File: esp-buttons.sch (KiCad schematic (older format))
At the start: 33 parts, among them Q1 FDV304P, U1 ESP-07v2, U2 LD1117S33CTR

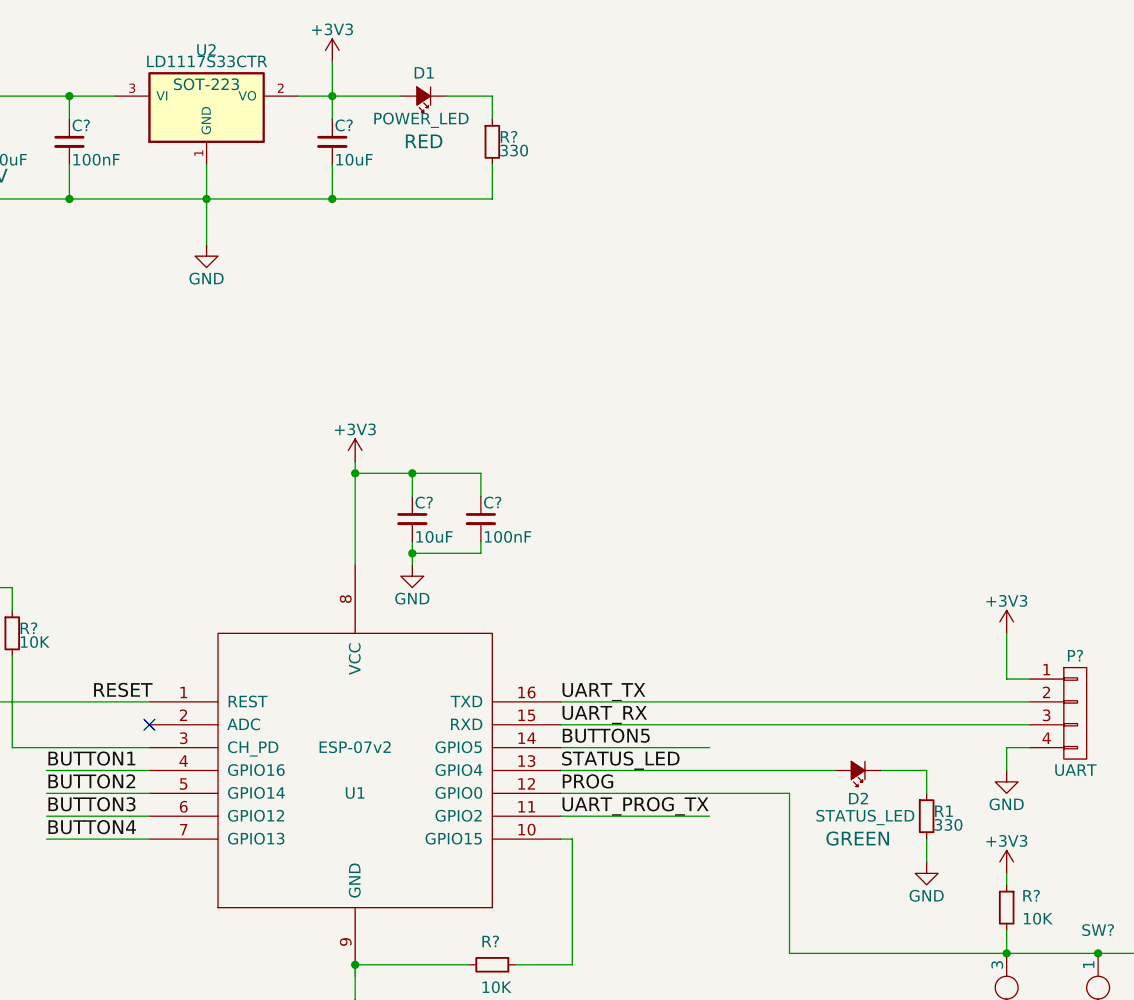
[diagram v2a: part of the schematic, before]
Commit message: Changed the value of the LEDs' resistors to give aproximately 5 mA of current to the LEDs. Changed the package of the SMD regulator (LD1117ADT33TR) from SOT-223 to TO-263 (D-PAK) for increased power dissipation
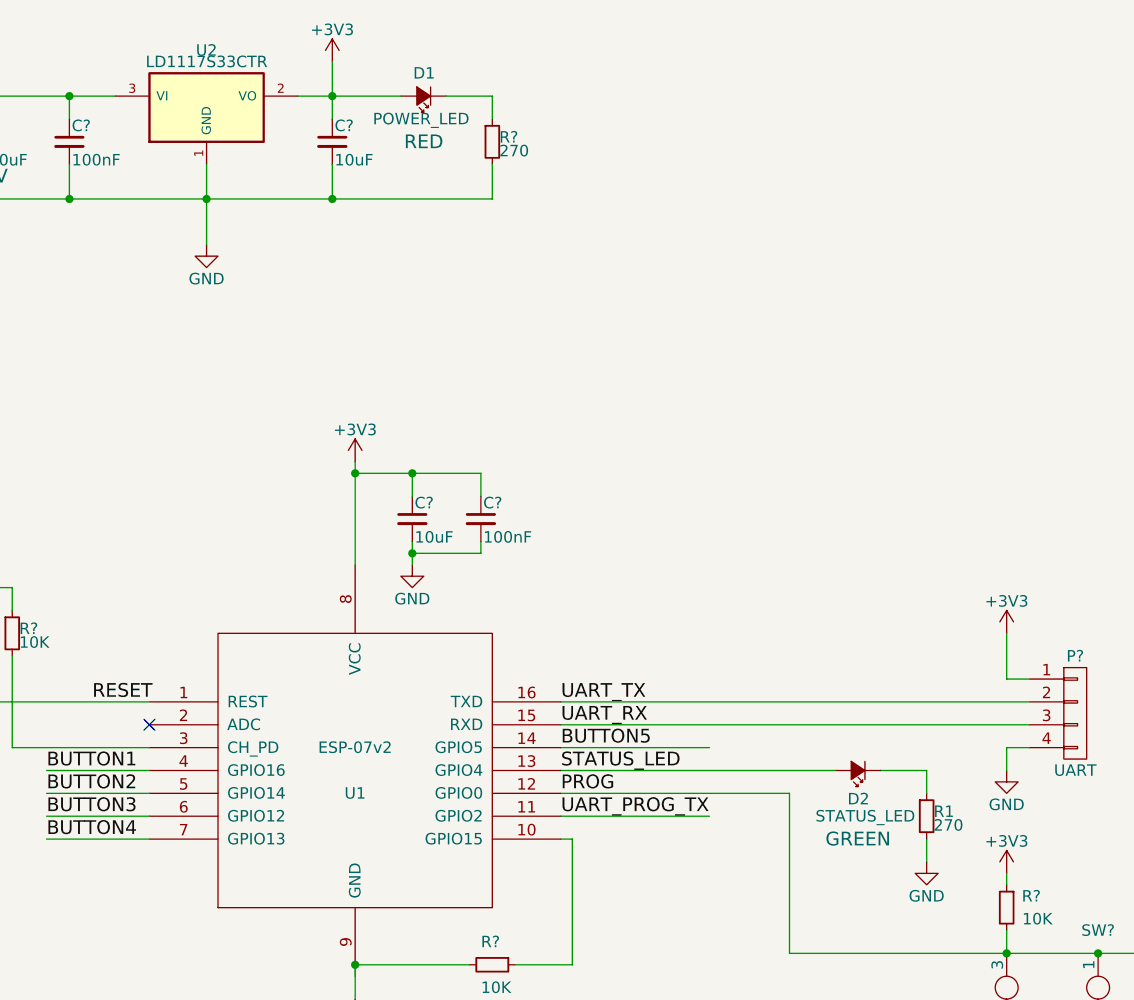
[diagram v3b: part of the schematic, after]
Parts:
- D1: Component (none) -> KPT-3216ID
- D2: Component (none) -> KPT-3216SGD
- R1, R?: value 330 -> 270
- U2: footprint SOT-223 -> TO_SOT_Packages_SMD:TO-263-3Lead; Component (none) -> LD1117ADT33TR
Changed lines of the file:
@@
 F 0 "U2" H 2850 1400 50  0000 C CNN
 F 1 "LD1117S33CTR" H 2850 1350 50  0000 C CNN
-F 2 "SOT-223" H 2850 1250 50  0000 C CNN
+F 2 "TO_SOT_Packages_SMD:TO-263-3Lead" H 2850 1250 50  0001 C CNN
 F 3 "" H 2850 1150 50  0000 C CNN
+F 4 "LD1117ADT33TR" H 2850 1150 60  0001 C CNN "Component"
 	1    2850 1150
 	1    0    0    -1
@@
 $EndComp
 $Comp
-L GND #PWR?
+L GND #PWR01
 U 1 1 57C6B0CF
 P 2850 1750
-F 0 "#PWR?" H 2850 1500 50  0001 C CNN
+F 0 "#PWR01" H 2850 1500 50  0001 C CNN
 F 1 "GND" H 2850 1600 50  0000 C CNN
 F 2 "" H 2850 1750 50  0000 C CNN
@@
 $EndComp
 $Comp
-L GND #PWR?
+L GND #PWR02
 U 1 1 57C6B187
 P 3500 5050
-F 0 "#PWR?" H 3500 4800 50  0001 C CNN
+F 0 "#PWR02" H 3500 4800 50  0001 C CNN
 F 1 "GND" H 3500 4900 50  0000 C CNN
 F 2 "" H 3500 5050 50  0000 C CNN
@@
 $EndComp
 $Comp
-L +3V3 #PWR?
+L +3V3 #PWR03
 U 1 1 57C6B1D7
 P 3500 2700
-F 0 "#PWR?" H 3500 2550 50  0001 C CNN
+F 0 "#PWR03" H 3500 2550 50  0001 C CNN
 F 1 "+3V3" H 3500 2840 50  0000 C CNN
 F 2 "" H 3500 2700 50  0000 C CNN
@@
 $EndComp
 $Comp
-L +5V #PWR?
+L +5V #PWR04
 U 1 1 57C6B214
 P 1800 950
-F 0 "#PWR?" H 1800 800 50  0001 C CNN
+F 0 "#PWR04" H 1800 800 50  0001 C CNN
 F 1 "+5V" H 1800 1090 50  0000 C CNN
 F 2 "" H 1800 950 50  0000 C CNN
@@
 $EndComp
 $Comp
-L GND #PWR?
+L GND #PWR05
 U 1 1 57C6B359
 P 3750 3150
-F 0 "#PWR?" H 3750 2900 50  0001 C CNN
+F 0 "#PWR05" H 3750 2900 50  0001 C CNN
 F 1 "GND" H 3750 3000 50  0000 C CNN
 F 2 "" H 3750 3150 50  0000 C CNN
@@
 $EndComp
 $Comp
-L +3V3 #PWR?
+L +3V3 #PWR06
 U 1 1 57C6B4E2
 P 3400 950
-F 0 "#PWR?" H 3400 800 50  0001 C CNN
+F 0 "#PWR06" H 3400 800 50  0001 C CNN
 F 1 "+3V3" H 3400 1090 50  0000 C CNN
 F 2 "" H 3400 950 50  0000 C CNN
@@
 $EndComp
 $Comp
-L +3V3 #PWR?
+L +3V3 #PWR07
 U 1 1 57C6C16A
 P 8700 1250
-F 0 "#PWR?" H 8700 1100 50  0001 C CNN
+F 0 "#PWR07" H 8700 1100 50  0001 C CNN
 F 1 "+3V3" H 8700 1390 50  0000 C CNN
 F 2 "" H 8700 1250 50  0000 C CNN
@@
 $EndComp
 $Comp
-L GND #PWR?
+L GND #PWR08
 U 1 1 57C6C1F6
 P 8300 1850
-F 0 "#PWR?" H 8300 1600 50  0001 C CNN
+F 0 "#PWR08" H 8300 1600 50  0001 C CNN
 F 1 "GND" H 8300 1700 50  0000 C CNN
 F 2 "" H 8300 1850 50  0000 C CNN
@@
 F 3 "" V 5700 4050 50  0000 C CNN
 F 4 "GREEN" H 5700 4350 60  0000 C CNN "Color"
+F 5 "KPT-3216SGD" H 5700 4050 60  0001 C CNN "Component"
 	1    5700 4050
 	-1   0    0    1
@@
 P 6000 4250
 F 0 "R1" H 6030 4270 50  0000 L CNN
-F 1 "330" H 6030 4210 50  0000 L CNN
+F 1 "270" H 6030 4210 50  0000 L CNN
 F 2 "Resistors_SMD:R_1206_HandSoldering" H 6000 4250 50  0001 C CNN
 F 3 "" H 6000 4250 50  0000 C CNN
@@
 $EndComp
 $Comp
-L +3V3 #PWR?
+L +3V3 #PWR09
 U 1 1 57C6CB01
 P 10400 2150
-F 0 "#PWR?" H 10400 2000 50  0001 C CNN
+F 0 "#PWR09" H 10400 2000 50  0001 C CNN
 F 1 "+3V3" H 10400 2290 50  0000 C CNN
 F 2 "" H 10400 2150 50  0000 C CNN
@@
 $EndComp
 $Comp
-L GND #PWR?
+L GND #PWR010
 U 1 1 57C6CB07
 P 10400 2900
-F 0 "#PWR?" H 10400 2650 50  0001 C CNN
+F 0 "#PWR010" H 10400 2650 50  0001 C CNN
 F 1 "GND" H 10400 2750 50  0000 C CNN
 F 2 "" H 10400 2900 50  0000 C CNN
@@
 $EndComp
 $Comp
-L +3V3 #PWR?
+L +3V3 #PWR011
 U 1 1 57C6CBE4
 P 8950 3400
-F 0 "#PWR?" H 8950 3250 50  0001 C CNN
+F 0 "#PWR011" H 8950 3250 50  0001 C CNN
 F 1 "+3V3" H 8950 3540 50  0000 C CNN
 F 2 "" H 8950 3400 50  0000 C CNN
@@
 $EndComp
 $Comp
-L GND #PWR?
+L GND #PWR012
 U 1 1 57C6CBEA
 P 8950 4150
-F 0 "#PWR?" H 8950 3900 50  0001 C CNN
+F 0 "#PWR012" H 8950 3900 50  0001 C CNN
 F 1 "GND" H 8950 4000 50  0000 C CNN
 F 2 "" H 8950 4150 50  0000 C CNN
@@
 $EndComp
 $Comp
-L +3V3 #PWR?
+L +3V3 #PWR013
 U 1 1 57C6CC7B
 P 10400 3400
-F 0 "#PWR?" H 10400 3250 50  0001 C CNN
+F 0 "#PWR013" H 10400 3250 50  0001 C CNN
 F 1 "+3V3" H 10400 3540 50  0000 C CNN
 F 2 "" H 10400 3400 50  0000 C CNN
@@
 $EndComp
 $Comp
-L GND #PWR?
+L GND #PWR014
 U 1 1 57C6CC81
 P 10400 4150
-F 0 "#PWR?" H 10400 3900 50  0001 C CNN
+F 0 "#PWR014" H 10400 3900 50  0001 C CNN
 F 1 "GND" H 10400 4000 50  0000 C CNN
 F 2 "" H 10400 4150 50  0000 C CNN
@@
 $EndComp
 $Comp
-L +3V3 #PWR?
+L +3V3 #PWR015
 U 1 1 57C6CD24
 P 8950 4650
-F 0 "#PWR?" H 8950 4500 50  0001 C CNN
+F 0 "#PWR015" H 8950 4500 50  0001 C CNN
 F 1 "+3V3" H 8950 4790 50  0000 C CNN
 F 2 "" H 8950 4650 50  0000 C CNN
@@
 $EndComp
 $Comp
-L GND #PWR?
+L GND #PWR016
 U 1 1 57C6CD2A
 P 8950 5400
-F 0 "#PWR?" H 8950 5150 50  0001 C CNN
+F 0 "#PWR016" H 8950 5150 50  0001 C CNN
 F 1 "GND" H 8950 5250 50  0000 C CNN
 F 2 "" H 8950 5400 50  0000 C CNN
@@
 $EndComp
 $Comp
-L +3V3 #PWR?
+L +3V3 #PWR017
 U 1 1 57C6D318
 P 1450 3200
-F 0 "#PWR?" H 1450 3050 50  0001 C CNN
+F 0 "#PWR017" H 1450 3050 50  0001 C CNN
 F 1 "+3V3" H 1450 3340 50  0000 C CNN
 F 2 "" H 1450 3200 50  0000 C CNN
@@
 $EndComp
 $Comp
-L GND #PWR?
+L GND #PWR018
 U 1 1 57C6D78B
 P 1450 4550
-F 0 "#PWR?" H 1450 4300 50  0001 C CNN
+F 0 "#PWR018" H 1450 4300 50  0001 C CNN
 F 1 "GND" H 1450 4400 50  0000 C CNN
 F 2 "" H 1450 4550 50  0000 C CNN
@@
 $EndComp
 $Comp
-L GND #PWR?
+L GND #PWR019
 U 1 1 57C70472
 P 6000 4450
-F 0 "#PWR?" H 6000 4200 50  0001 C CNN
+F 0 "#PWR019" H 6000 4200 50  0001 C CNN
 F 1 "GND" H 6000 4300 50  0000 C CNN
 F 2 "" H 6000 4450 50  0000 C CNN
@@
 F 3 "" V 3800 1100 50  0000 C CNN
 F 4 "RED" H 3800 1300 60  0000 C CNN "Color"
+F 5 "KPT-3216ID" H 3800 1100 60  0001 C CNN "Component"
 	1    3800 1100
 	-1   0    0    1
@@
 P 4100 1300
 F 0 "R?" H 4130 1320 50  0000 L CNN
-F 1 "330" H 4130 1260 50  0000 L CNN
+F 1 "270" H 4130 1260 50  0000 L CNN
 F 2 "Resistors_SMD:R_1206_HandSoldering" H 4100 1300 50  0001 C CNN
 F 3 "" H 4100 1300 50  0000 C CNN
@@
 $EndComp
 $Comp
-L +5V #PWR?
+L +5V #PWR020
 U 1 1 57C714FA
 P 7950 1050
-F 0 "#PWR?" H 7950 900 50  0001 C CNN
+F 0 "#PWR020" H 7950 900 50  0001 C CNN
 F 1 "+5V" H 7950 1190 50  0000 C CNN
 F 2 "" H 7950 1050 50  0000 C CNN
@@
 $EndComp
 $Comp
-L GND #PWR?
+L GND #PWR021
 U 1 1 57C71A7A
 P 8650 2450
-F 0 "#PWR?" H 8650 2200 50  0001 C CNN
+F 0 "#PWR021" H 8650 2200 50  0001 C CNN
 F 1 "GND" H 8650 2300 50  0000 C CNN
 F 2 "" H 8650 2450 50  0000 C CNN
@@
 $EndComp
 $Comp
-L GND #PWR?
+L GND #PWR022
 U 1 1 57C82907
 P 6350 4050
-F 0 "#PWR?" H 6350 3800 50  0001 C CNN
+F 0 "#PWR022" H 6350 3800 50  0001 C CNN
 F 1 "GND" H 6350 3900 50  0000 C CNN
 F 2 "" H 6350 4050 50  0000 C CNN
@@
 $EndComp
 $Comp
-L +3V3 #PWR?
+L +3V3 #PWR023
 U 1 1 57C82955
 P 6350 3450
-F 0 "#PWR?" H 6350 3300 50  0001 C CNN
+F 0 "#PWR023" H 6350 3300 50  0001 C CNN
 F 1 "+3V3" H 6350 3590 50  0000 C CNN
 F 2 "" H 6350 3450 50  0000 C CNN
@@
 $EndComp
 $Comp
-L +3V3 #PWR?
+L +3V3 #PWR024
 U 1 1 57C83F12
 P 6350 4500
-F 0 "#PWR?" H 6350 4350 50  0001 C CNN
+F 0 "#PWR024" H 6350 4350 50  0001 C CNN
 F 1 "+3V3" H 6350 4640 50  0000 C CNN
 F 2 "" H 6350 4500 50  0000 C CNN
@@
 $EndComp
 $Comp
-L GND #PWR?
+L GND #PWR025
 U 1 1 57C83F22
 P 6350 5650
-F 0 "#PWR?" H 6350 5400 50  0001 C CNN
+F 0 "#PWR025" H 6350 5400 50  0001 C CNN
 F 1 "GND" H 6350 5500 50  0000 C CNN
 F 2 "" H 6350 5650 50  0000 C CNN

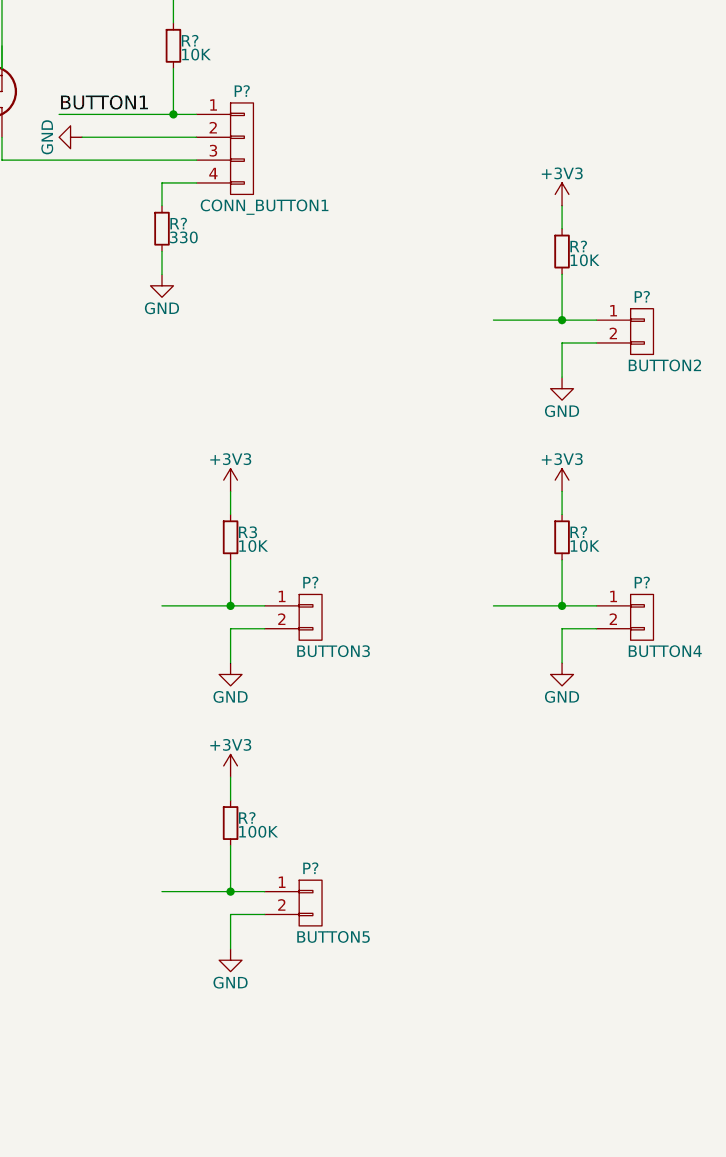
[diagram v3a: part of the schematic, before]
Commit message: Removed the temporary buttons' circuits
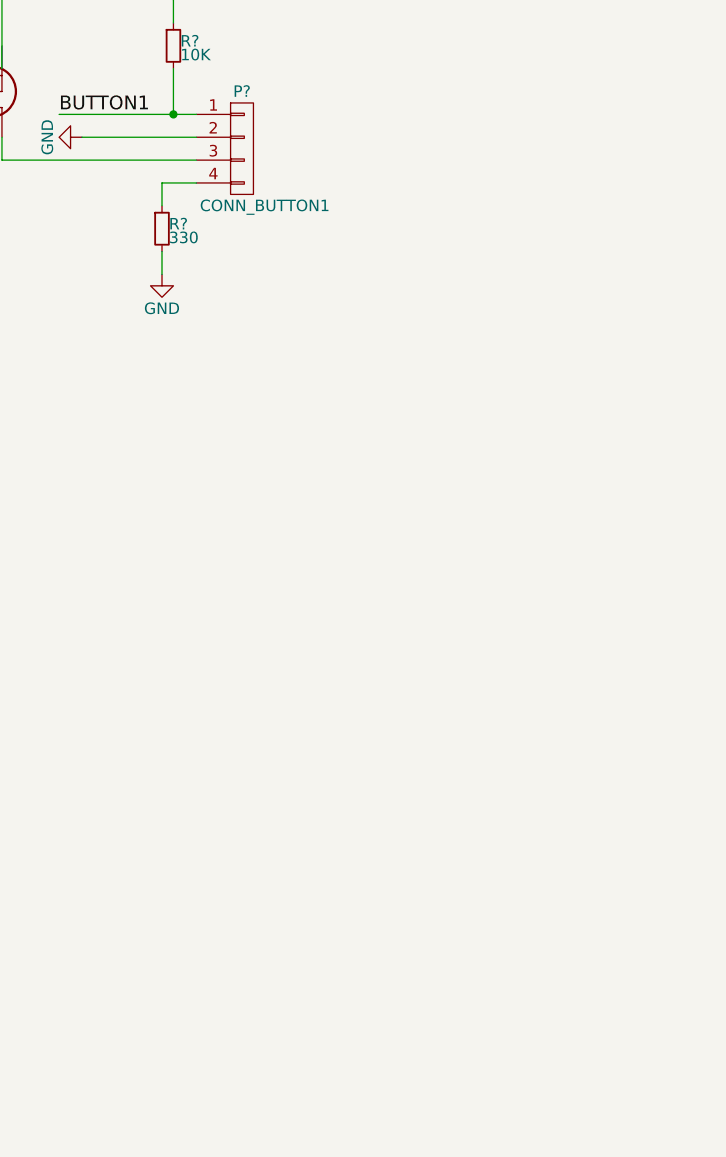
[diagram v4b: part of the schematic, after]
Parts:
- removed P?: BUTTON2, symbol CONN_01X02
- removed P?: BUTTON3, symbol CONN_01X02
- removed P?: BUTTON4, symbol CONN_01X02
- removed P?: BUTTON5, symbol CONN_01X02
- removed R3, R? (x2): 10K, Resistors_SMD:R_1206_HandSoldering, symbol R_Small
- removed R?: 100K, Resistors_SMD:R_1206_HandSoldering, symbol R_Small
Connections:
- wire segments 117 -> 93
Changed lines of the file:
@@
-$EndComp
-$Comp
-L CONN_01X02 P?
-U 1 1 57C6CAF5
-P 10750 2700
-F 0 "P?" H 10750 2850 50  0000 C CNN
-F 1 "BUTTON2" H 10850 2550 50  0000 C CNN
-F 2 "" H 10750 2700 50  0000 C CNN
-F 3 "" H 10750 2700 50  0000 C CNN
-	1    10750 2700
-	1    0    0    -1
-$EndComp
-$Comp
-L R_Small R?
-U 1 1 57C6CAFB
-P 10400 2350
-F 0 "R?" H 10430 2370 50  0000 L CNN
-F 1 "10K" H 10430 2310 50  0000 L CNN
-F 2 "Resistors_SMD:R_1206_HandSoldering" H 10400 2350 50  0001 C CNN
-F 3 "" H 10400 2350 50  0000 C CNN
-	1    10400 2350
-	1    0    0    -1
-$EndComp
-$Comp
-L +3V3 #PWR09
-U 1 1 57C6CB01
-P 10400 2150
-F 0 "#PWR09" H 10400 2000 50  0001 C CNN
-F 1 "+3V3" H 10400 2290 50  0000 C CNN
-F 2 "" H 10400 2150 50  0000 C CNN
-F 3 "" H 10400 2150 50  0000 C CNN
-	1    10400 2150
-	1    0    0    -1
-$EndComp
-$Comp
-L GND #PWR010
-U 1 1 57C6CB07
-P 10400 2900
-F 0 "#PWR010" H 10400 2650 50  0001 C CNN
-F 1 "GND" H 10400 2750 50  0000 C CNN
-F 2 "" H 10400 2900 50  0000 C CNN
-F 3 "" H 10400 2900 50  0000 C CNN
-	1    10400 2900
-	1    0    0    -1
-$EndComp
-$Comp
-L CONN_01X02 P?
-U 1 1 57C6CBD8
-P 9300 3950
-F 0 "P?" H 9300 4100 50  0000 C CNN
-F 1 "BUTTON3" H 9400 3800 50  0000 C CNN
-F 2 "" H 9300 3950 50  0000 C CNN
-F 3 "" H 9300 3950 50  0000 C CNN
-	1    9300 3950
-	1    0    0    -1
-$EndComp
-$Comp
-L R_Small R3
-U 1 1 57C6CBDE
-P 8950 3600
-F 0 "R3" H 8980 3620 50  0000 L CNN
-F 1 "10K" H 8980 3560 50  0000 L CNN
-F 2 "Resistors_SMD:R_1206_HandSoldering" H 8950 3600 50  0001 C CNN
-F 3 "" H 8950 3600 50  0000 C CNN
-	1    8950 3600
-	1    0    0    -1
-$EndComp
-$Comp
-L +3V3 #PWR011
-U 1 1 57C6CBE4
-P 8950 3400
-F 0 "#PWR011" H 8950 3250 50  0001 C CNN
-F 1 "+3V3" H 8950 3540 50  0000 C CNN
-F 2 "" H 8950 3400 50  0000 C CNN
-F 3 "" H 8950 3400 50  0000 C CNN
-	1    8950 3400
-	1    0    0    -1
-$EndComp
-$Comp
-L GND #PWR012
-U 1 1 57C6CBEA
-P 8950 4150
-F 0 "#PWR012" H 8950 3900 50  0001 C CNN
-F 1 "GND" H 8950 4000 50  0000 C CNN
-F 2 "" H 8950 4150 50  0000 C CNN
-F 3 "" H 8950 4150 50  0000 C CNN
-	1    8950 4150
-	1    0    0    -1
-$EndComp
-$Comp
-L CONN_01X02 P?
-U 1 1 57C6CC6F
-P 10750 3950
-F 0 "P?" H 10750 4100 50  0000 C CNN
-F 1 "BUTTON4" H 10850 3800 50  0000 C CNN
-F 2 "" H 10750 3950 50  0000 C CNN
-F 3 "" H 10750 3950 50  0000 C CNN
-	1    10750 3950
-	1    0    0    -1
-$EndComp
-$Comp
-L R_Small R?
-U 1 1 57C6CC75
-P 10400 3600
-F 0 "R?" H 10430 3620 50  0000 L CNN
-F 1 "10K" H 10430 3560 50  0000 L CNN
-F 2 "Resistors_SMD:R_1206_HandSoldering" H 10400 3600 50  0001 C CNN
-F 3 "" H 10400 3600 50  0000 C CNN
-	1    10400 3600
-	1    0    0    -1
-$EndComp
-$Comp
-L +3V3 #PWR013
-U 1 1 57C6CC7B
-P 10400 3400
-F 0 "#PWR013" H 10400 3250 50  0001 C CNN
-F 1 "+3V3" H 10400 3540 50  0000 C CNN
-F 2 "" H 10400 3400 50  0000 C CNN
-F 3 "" H 10400 3400 50  0000 C CNN
-	1    10400 3400
-	1    0    0    -1
-$EndComp
-$Comp
-L GND #PWR014
-U 1 1 57C6CC81
-P 10400 4150
-F 0 "#PWR014" H 10400 3900 50  0001 C CNN
-F 1 "GND" H 10400 4000 50  0000 C CNN
-F 2 "" H 10400 4150 50  0000 C CNN
-F 3 "" H 10400 4150 50  0000 C CNN
-	1    10400 4150
-	1    0    0    -1
-$EndComp
-$Comp
-L CONN_01X02 P?
-U 1 1 57C6CD18
-P 9300 5200
-F 0 "P?" H 9300 5350 50  0000 C CNN
-F 1 "BUTTON5" H 9400 5050 50  0000 C CNN
-F 2 "" H 9300 5200 50  0000 C CNN
-F 3 "" H 9300 5200 50  0000 C CNN
-	1    9300 5200
-	1    0    0    -1
-$EndComp
-$Comp
-L R_Small R?
-U 1 1 57C6CD1E
-P 8950 4850
-F 0 "R?" H 8980 4870 50  0000 L CNN
-F 1 "100K" H 8980 4810 50  0000 L CNN
-F 2 "Resistors_SMD:R_1206_HandSoldering" H 8950 4850 50  0001 C CNN
-F 3 "" H 8950 4850 50  0000 C CNN
-	1    8950 4850
-	1    0    0    -1
-$EndComp
-$Comp
-L +3V3 #PWR015
-U 1 1 57C6CD24
-P 8950 4650
-F 0 "#PWR015" H 8950 4500 50  0001 C CNN
-F 1 "+3V3" H 8950 4790 50  0000 C CNN
-F 2 "" H 8950 4650 50  0000 C CNN
-F 3 "" H 8950 4650 50  0000 C CNN
-	1    8950 4650
-	1    0    0    -1
-$EndComp
-$Comp
-L GND #PWR016
-U 1 1 57C6CD2A
-P 8950 5400
-F 0 "#PWR016" H 8950 5150 50  0001 C CNN
-F 1 "GND" H 8950 5250 50  0000 C CNN
-F 2 "" H 8950 5400 50  0000 C CNN
-F 3 "" H 8950 5400 50  0000 C CNN
-	1    8950 5400
-	1    0    0    -1
 $EndComp
 $Comp
@@
 Connection ~ 3400 1550
 Wire Wire Line
-	10400 2450 10400 2650
-Wire Wire Line
-	10100 2650 10400 2650
-Wire Wire Line
-	10400 2650 10550 2650
-Wire Wire Line
-	10400 2150 10400 2250
-Wire Wire Line
-	10550 2750 10400 2750
-Wire Wire Line
-	10400 2750 10400 2900
-Connection ~ 10400 2650
-Wire Wire Line
-	8950 3700 8950 3900
-Wire Wire Line
-	8650 3900 8950 3900
-Wire Wire Line
-	8950 3900 9100 3900
-Wire Wire Line
-	8950 3400 8950 3500
-Wire Wire Line
-	9100 4000 8950 4000
-Wire Wire Line
-	8950 4000 8950 4150
-Connection ~ 8950 3900
-Wire Wire Line
-	10400 3700 10400 3900
-Wire Wire Line
-	10100 3900 10400 3900
-Wire Wire Line
-	10400 3900 10550 3900
-Wire Wire Line
-	10400 3400 10400 3500
-Wire Wire Line
-	10550 4000 10400 4000
-Wire Wire Line
-	10400 4000 10400 4150
-Connection ~ 10400 3900
-Wire Wire Line
-	8950 4950 8950 5150
-Wire Wire Line
-	8650 5150 8950 5150
-Wire Wire Line
-	8950 5150 9100 5150
-Wire Wire Line
-	8950 4650 8950 4750
-Wire Wire Line
-	9100 5250 8950 5250
-Wire Wire Line
-	8950 5250 8950 5400
-Connection ~ 8950 5150
-Wire Wire Line
 	1450 3200 1450 3250
